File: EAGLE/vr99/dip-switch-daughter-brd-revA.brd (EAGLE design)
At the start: 40 x 9 mm, 9 parts

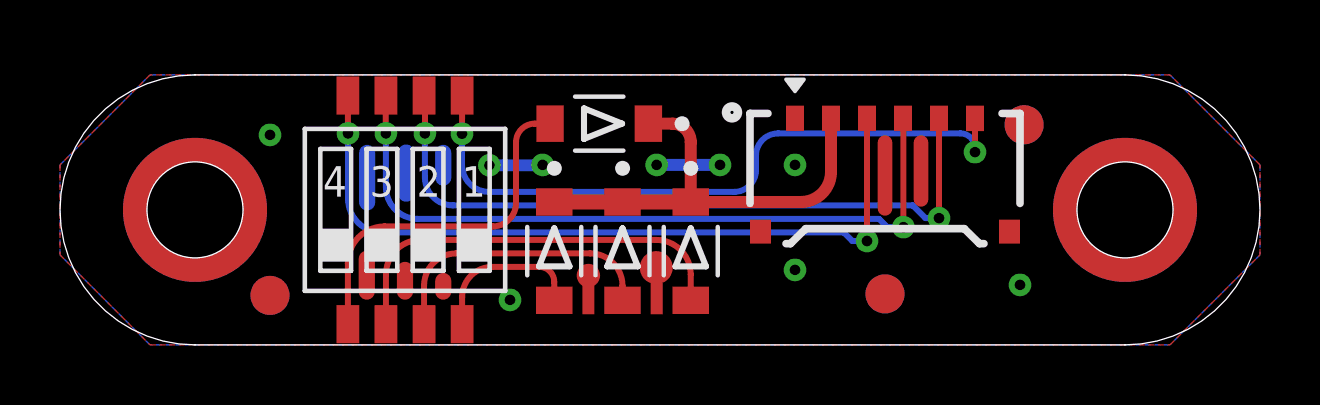
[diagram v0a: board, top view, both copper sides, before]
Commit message: DIP Switch DB
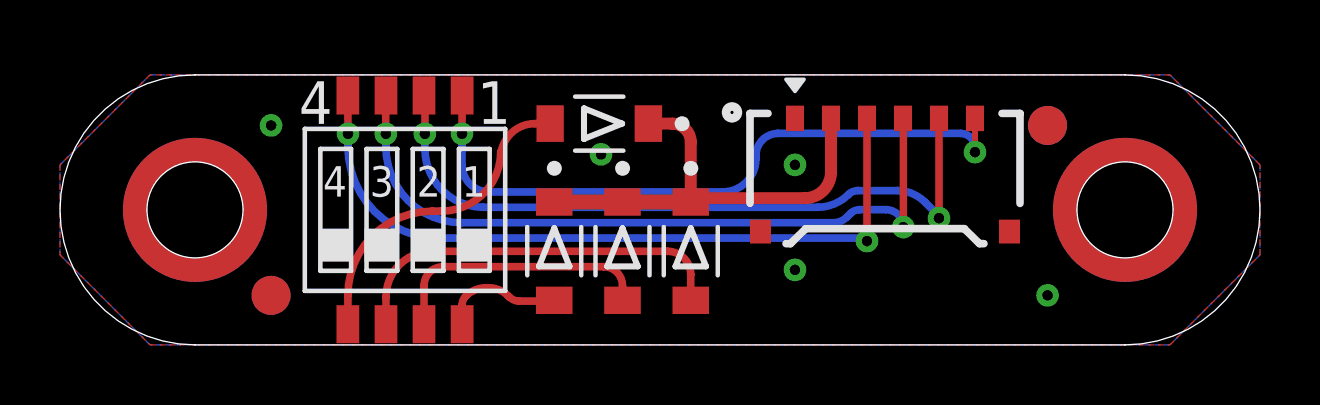
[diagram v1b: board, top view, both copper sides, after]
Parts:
- removed U$1, U$2, U$7: FIDUCIAL, __temp_to_delete:FIDUCIAL
- added F1, F2: FIDUCIAL, __temp_to_delete:FIDUCIAL
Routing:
- net X: track 10.1 -> 0.00 mm
- net GND: track 3.89 -> 0.00 mm, vias 9 -> 5
- net N$5: track 11.9 -> 10.3 mm
- net N$8: track 5.21 -> 4.07 mm
- net COL3: track 25.4 -> 24.4 mm
- net N$6: track 13.6 -> 12.9 mm
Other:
- board text added: "1"
- board text added: "4"
